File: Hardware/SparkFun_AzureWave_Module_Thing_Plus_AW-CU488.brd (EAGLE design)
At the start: 22.9 x 77.5 mm, 123 parts, among them J1 THING_PLUS, J3 QWIIC_RA, J5 USB-C, Q1 3.1A/30V/105mΩ, Q2 MBT3904DW1T1, U2 CP210X, U3 AP2112K-3.3V, U4 MCP73831

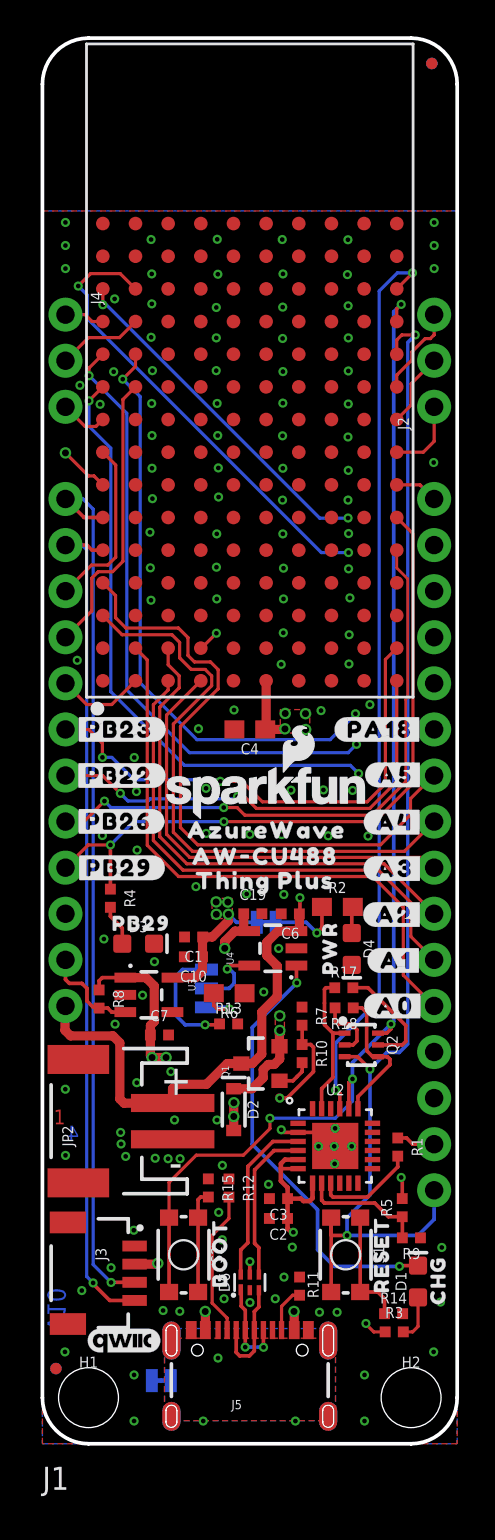
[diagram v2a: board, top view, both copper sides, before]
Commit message: changes found during proto testing
-removed R14 pulldown on reset button. It now pulls down directly to GND when pressed.
-adjusted Charge LED resistor to lower brightness (R3 changed from 1K to 4.7K)
-Added PTH header breakouts for UART LOG RX and TX.
-Changed silk on all pins to more user-friendly/common digital numbers.
-Added jumpers to more easily remove auto-boot circuit if needed for advanced use cases
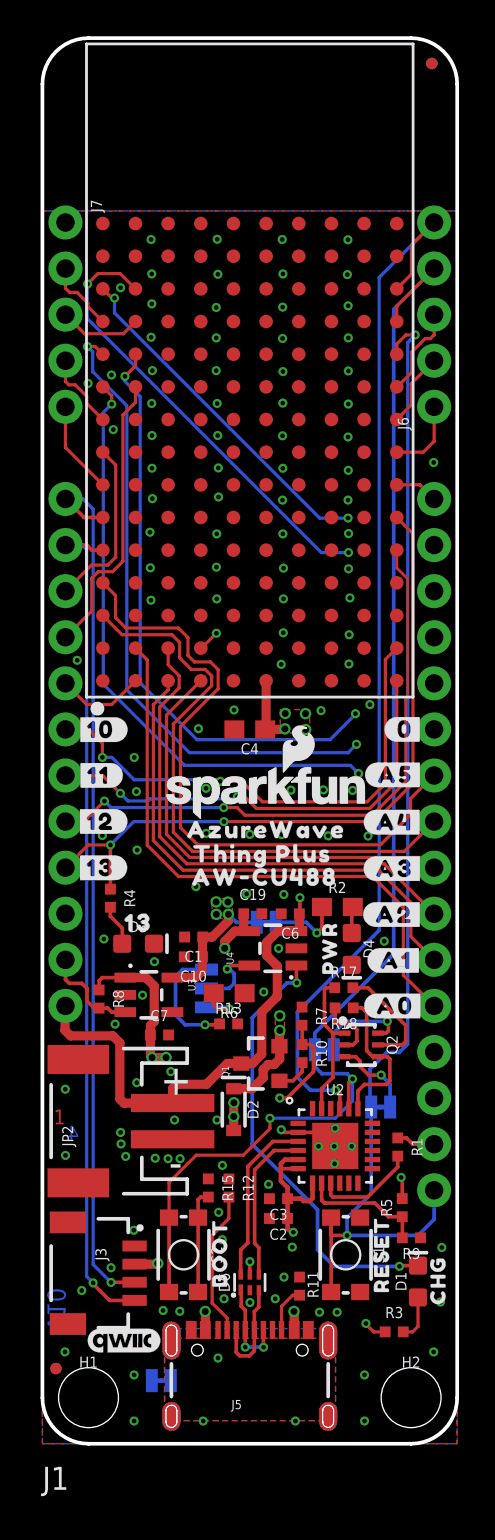
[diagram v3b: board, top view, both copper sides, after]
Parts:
- removed J2, J4: (no value), SparkFun-Connectors:1X03_NO_SILK
- removed R14: 10k, SparkFun-Resistors:0402-TIGHT
- removed TP1: (no value), SparkFun-Connectors:TP_15TH
- removed U$19: (no value), output:#PA4#32
- removed U$21: (no value), output:#PA2#32
- removed U$22: (no value), output:#PA14#32
- removed U$24: (no value), output:#PA15#32
- removed U$25: (no value), output:#PA26#SDA#32
- removed U$26: (no value), output:#PA25#SCL#32
- removed U$28: (no value), output:#PA30#32
- removed U$30: (no value), output:#PB3#A6#0
- removed U$31: (no value), output:#PA19#CS#32
- removed U$33: (no value), output:#PA27#32
- removed U$34: (no value), output:#PB23#32
- removed U$35: (no value), output:PB290
- removed U$36: (no value), output:#PB22#32
- removed U$37: (no value), output:#PB26#32
- removed U$38: (no value), output:#PB29#32
- removed U$39: (no value), output:#PA18#SCK#19
- removed U$40: (no value), output:#PA16#PICO#19
- removed U$44: (no value), output:#NC#0
- removed U$47: (no value), output:#PA17#POCI#19
- removed U$51: (no value), output:#PB4#A0#5
- removed U$52: (no value), output:#PB5#A1#5
- removed U$58: (no value), output:#PA18#6
- removed U$61: (no value), output:#PB6#A2#19
- removed U$63: (no value), output:#PB7#A3#19
- removed U$65: (no value), output:#PB1#A4#19
- removed U$66: (no value), output:#PB2#A5#19
- added J6, J7: (no value), SparkFun-Connectors:1X05_NO_SILK
- added JP1, JP3: (no value), SparkFun-Jumpers:SMT-JUMPER_2_NC_TRACE_SILK
- added U$48: (no value), output:#4#TX1#14
- added U$49: (no value), output:#3#RX1#14
- added U$50: (no value), output:#2#POCI#14
- added U$64: (no value), output:#1#PICO#14
- added U$67: (no value), output:#13#14
- added U$68: (no value), output:#12#14
- added U$69: (no value), output:#11#14
- added U$70: (no value), output:#10#14
- added U$71: (no value), output:#9#A6#14
- added U$72: (no value), output:#8#CS#14
- added U$73: (no value), output:#7#14
- added U$74: (no value), output:#6#SCL#14
- added U$75: (no value), output:#5#SDA#14
- added U$76: (no value), output:#0#SCK#14
- added U$77: (no value), output:#14#A0#15
- added U$80: (no value), output:#15#A1#15
- added U$81: (no value), output:#16#A2#16
- added U$82: (no value), output:#17#A3#17
- added U$83: (no value), output:#18#A4#18
- added U$84: (no value), output:#19#A5#19
- added U$85: (no value), output:#20#20
- added U$86: (no value), output:#GND#0
- added U$87: (no value), output:#21#21
- added U$88: (no value), output:#22#22
- added U$89: (no value), output:#23#23
- added U$90: (no value), output:#24#TX#24
- added U$91: (no value), output:#25#RX#25
- added U$92: (no value), output:#26#26
- added U$93: (no value), output:#27#27
- added U$94: (no value), output:#28#28
- added U$95: (no value), output:#29#29
- R3: value 1k -> 4.7k
- U$1: device output:#PA13#RXD#19 -> output:#10#30
- U$12: device output:#PA0#32 -> output:#12#30
- U$14: device output:#PB31#19 -> output:#13#30
- U$15: device output:#PB26#30 -> output:#JP1#1
- U$16: device output:#PB22#30 -> output:#0#1
- U$17: device output:#PB23#30 -> output:#JP3#2
- U$5: device output:#PA12#TXD#19 -> output:#11#30
- U$7: device output:#PB29#0 -> output:1330
- moved LOGO2 49.5 mm to (11.4, 10.2)
- moved U$12 27.7 mm to (3.21, 34.3), flipped to the top
- moved U$14 25.6 mm to (3.20, 31.7), flipped to the top
- moved U$15 19.6 mm to (15.9, 18.6), flipped to the bottom
- moved U$17 19.6 mm to (12.7, 21.7), flipped to the bottom
- moved U$5 18.5 mm to (3.10, 36.8), flipped to the top
- moved U$16 16.0 mm to (20.0, 39.4)
- moved U$1 15.4 mm to (3.22, 39.4), flipped to the top
- moved U$9 8.86 mm to (11.5, 56.6)
- moved U$8 7.87 mm to (11.4, 59.7)
- moved U$10 5.06 mm to (11.2, 58.2)
- moved U$7 3.22 mm to (5.29, 28.7)
- moved U$62 1.48 mm to (12.3, 32.5)
- moved U$27 1.15 mm to (12.4, 31.2)
- moved LOGO3 1.15 mm to (11.4, 71.4)
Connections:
- new net N$6: JP1.1, Q2.3
- net CHIP_EN: now also JP1.2; no longer Q2.3
- net GND: now also J7.1, S1.3, S1.4; no longer R14.2
- net N$10: now also JP3.1, Q2.6; no longer R14.1, S1.3, S1.4
- net PA0: now also J6.1; no longer J2.1
- net PA14: now also J7.2; no longer J4.1
- net PA15: now also J7.3; no longer J4.2
- net PA2: now also J6.3; no longer J2.3
- net PA27: now also J7.4; no longer J4.3
- net PA28: now also J7.5; no longer TP1.1
- net PA4: now also J6.2; no longer J2.2
- net PA7/UART-LOG-TXD: now also J6.4, JP3.2; no longer Q2.6
- net PA8/UART-LOG-RXD: now also J6.5
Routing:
- net PA8/UART-LOG-RXD: track 49.7 -> 58.3 mm, vias 2 -> 1
- net PA7/UART-LOG-TXD: track 67.2 -> 74.1 mm, vias 4 -> 2
- net N$6: track 0.00 -> 4.58 mm, vias 0 -> 1
- net PA28: track 2.79 -> 5.15 mm
- net PA14: track 2.22 -> 4.01 mm
- net CHIP_EN: track 67.9 -> 66.1 mm, vias 3 -> 2
- net PA27: track 2.67 -> 4.30 mm
- net PA16/PICO: track 39.6 -> 40.8 mm
- net N$10: track 6.42 -> 5.32 mm, vias 0 -> 1
- net RTS: track 7.88 -> 8.59 mm
- net LP_UART_RXD: track 31.1 -> 30.5 mm
- net GND: vias 134 -> 129

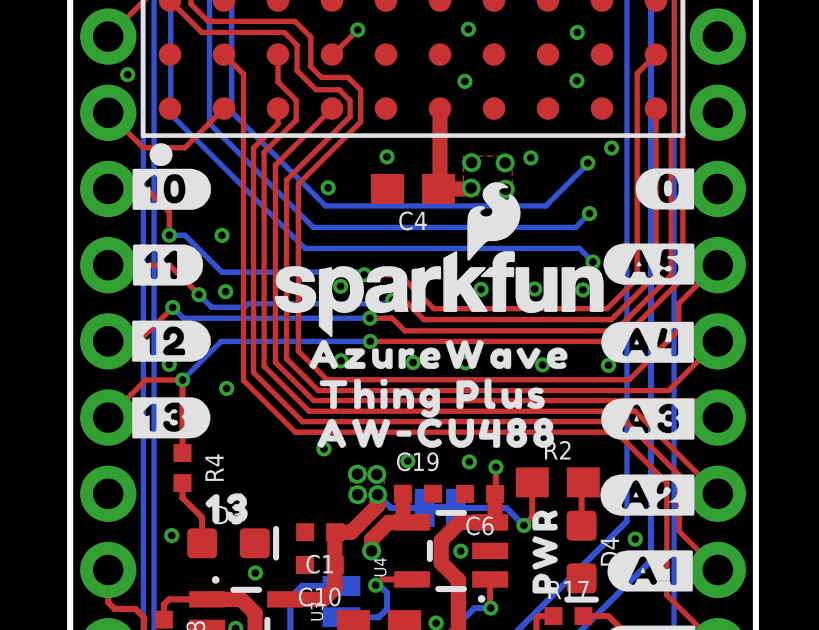
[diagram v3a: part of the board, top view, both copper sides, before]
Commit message: centered SFE logo and product name text
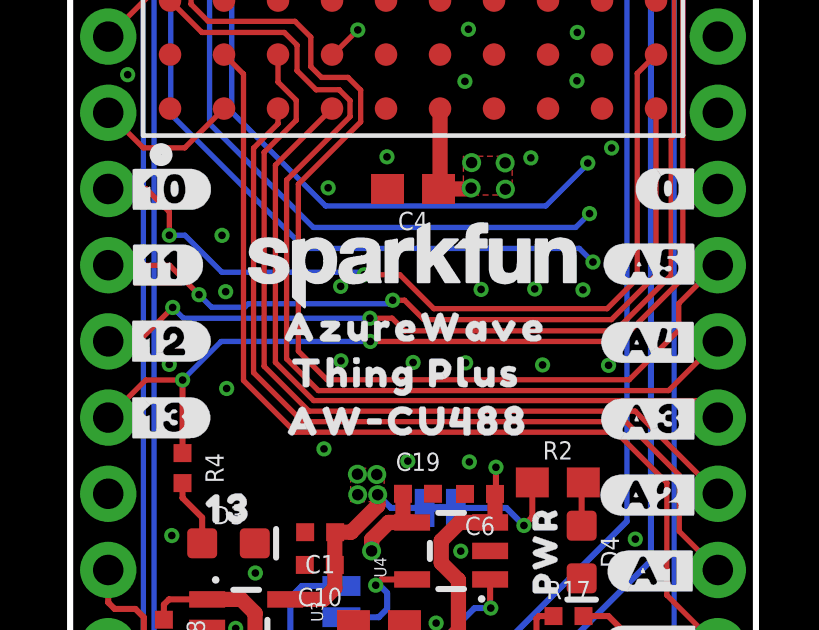
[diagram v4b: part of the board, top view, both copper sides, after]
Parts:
- removed LOGO3, LOGO5: SFE_LOGO_NAME_FLAME.1_INCH, SparkFun-Aesthetics:SFE_LOGO_NAME_FLAME_.1
- added LOGO1: SFE_LOGO_NAME.1_INCH, SparkFun-Aesthetics:SFE_LOGO_NAME_.1
- moved U$6 1.24 mm to (11.5, 34.8)
- moved U$62 1.17 mm to (11.4, 33.2)
- moved U$27 1.07 mm to (11.4, 31.6)
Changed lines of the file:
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@@
 <attribute name="VALUE" value="100k" x="2.697478125" y="24.546559375" size="0.6096" layer="27" font="vector" ratio="20" rot="R270" align="top-center"/>
 </element>
-<element name="LOGO3" library="SparkFun-Aesthetics" package="SFE_LOGO_NAME_FLAME_.1" value="SFE_LOGO_NAME_FLAME.1_INCH" x="11.43" y="71.371459375" smashed="yes" rot="MR0"/>
 <element name="LOGO4" library="SparkFun-Aesthetics" package="FOUR_LAYER_WARNING" value="FOUR_LAYER_WARNING" x="30.48" y="39.37" smashed="yes"/>
 <element name="U$59" library="SparkFun-Aesthetics" package="ORDERING_INSTRUCTIONS" value="" x="29.21" y="50.8" smashed="yes"/>
@@
 <element name="U$60" library="output" package="#100#0" value="" x="9.0297" y="26.41091875" smashed="yes" rot="MR90"/>
 <element name="U$4" library="output" package="#500#0" value="" x="9.0271625" y="23.7388375" smashed="yes" rot="MR90"/>
-<element name="U$62" library="output" package="THING_PLUS_0" value="" x="12.31138125" y="32.50945625" smashed="yes"/>
+<element name="U$62" library="output" package="THING_PLUS_0" value="" x="11.39444375" y="33.23335625" smashed="yes"/>
 <element name="R10" library="SparkFun-Resistors" package="0402-TIGHT" value="100" x="14.315440625" y="21.503640625" smashed="yes" rot="R270">
 <attribute name="NAME" x="15.077440625" y="21.503640625" size="0.6096" layer="25" font="vector" ratio="20" rot="R270" align="bottom-center"/>
@@
 <attribute name="VALUE" x="11.43" y="40.132" size="0.6096" layer="27" font="vector" ratio="20" rot="R180" align="top-center"/>
 </element>
-<element name="U$27" library="output" package="AW#CU488_0" value="" x="12.4307625" y="31.2166" smashed="yes"/>
+<element name="U$27" library="output" package="AW#CU488_0" value="" x="11.442703125" y="31.623" smashed="yes"/>
 <element name="U$2" library="output" package="BOOT0" value="" x="9.779" y="10.5156" smashed="yes" rot="R90"/>
-<element name="U$6" library="output" package="AZUREWAVE0" value="" x="12.346940625" y="33.842959375" smashed="yes"/>
+<element name="U$6" library="output" package="AZUREWAVE0" value="" x="11.521440625" y="34.762440625" smashed="yes"/>
 <element name="U$8" library="output" package="AZUREWAVE0" value="" x="11.43" y="59.69" smashed="yes" rot="MR0"/>
 <element name="U$9" library="output" package="AW#CU488_0" value="" x="11.452859375" y="56.57595625" smashed="yes" rot="MR0"/>
@@
 <element name="U$56" library="output" package="#A4#6" value="" x="19.4183" y="34.25698125" smashed="yes"/>
 <element name="U$57" library="output" package="#A5#6" value="" x="19.46401875" y="36.8655625" smashed="yes"/>
-<element name="LOGO5" library="SparkFun-Aesthetics" package="SFE_LOGO_NAME_FLAME_.1" value="SFE_LOGO_NAME_FLAME.1_INCH" x="12.38758125" y="35.892740625" smashed="yes"/>
 <element name="U$18" library="output" package="#A0#30" value="" x="19.453859375" y="24.127459375" smashed="yes"/>
 <element name="USBSHLD" library="SparkFun-Jumpers" package="SMT-JUMPER_2_NC_TRACE_SILK" package3d_urn="urn:adsk.eagle:package:39281/1" value="" x="6.5532" y="3.4798" smashed="yes" rot="MR180">
@@
 <element name="U$15" library="output" package="#JP1#1" value="" x="15.935959375" y="18.557240625" smashed="yes" rot="MR0"/>
 <element name="U$17" library="output" package="#JP3#2" value="" x="12.71778125" y="21.676359375" smashed="yes" rot="MR0"/>
+<element name="LOGO1" library="SparkFun-Aesthetics" package="SFE_LOGO_NAME_.1" value="SFE_LOGO_NAME.1_INCH" x="11.43" y="36.83" smashed="yes"/>
 </elements>
 <signals>

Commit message: Reds review catches
-added note in SCH about pwr LED jumper
-approved jumper overlap DRC errors
-added table lines to schematic info about auto-reset
-moved OSHW logo over via
-removed unncessary GND vias under USB-C
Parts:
- moved LOGO2 0.12 mm to (11.4, 10.0)
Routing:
- net GND: vias 129 -> 127
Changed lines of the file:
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@@
 <layer number="98" name="Guide" color="6" fill="1" visible="no" active="no"/>
 <layer number="99" name="SpiceOrder" color="7" fill="1" visible="no" active="no"/>
-<layer number="100" name="Muster" color="7" fill="1" visible="no" active="yes"/>
+<layer number="100" name="Muster" color="7" fill="1" visible="yes" active="yes"/>
 <layer number="101" name="Patch_Top" color="12" fill="4" visible="no" active="no"/>
 <layer number="102" name="Vscore" color="7" fill="1" visible="no" active="no"/>
@@
 <attribute name="VALUE" x="11.577315625" y="29.6926" size="0.6096" layer="27" font="vector" ratio="20" rot="R180" align="top-center"/>
 </element>
-<element name="LOGO2" library="SparkFun-Aesthetics" package="OSHW-LOGO-MINI" value="OSHW-LOGOMINI" x="11.43" y="10.16" smashed="yes" rot="MR0"/>
+<element name="LOGO2" library="SparkFun-Aesthetics" package="OSHW-LOGO-MINI" value="OSHW-LOGOMINI" x="11.43" y="10.0431625" smashed="yes" rot="MR0"/>
 <element name="J3" library="SparkFun-Connectors" package="JST04_1MM_RA" value="QWIIC_RA" x="5.08" y="9.398" smashed="yes" rot="R270">
 <attribute name="NAME" x="2.921" y="10.795" size="0.6096" layer="25" font="vector" ratio="20" rot="R270"/>
@@
 <via x="17.752059375" y="1.25221875" extent="1-16" drill="0.254"/>
 <via x="21.562059375" y="5.06221875" extent="1-16" drill="0.254"/>
-<via x="13.942059375" y="1.25221875" extent="1-16" drill="0.254"/>
-<via x="8.862059375" y="1.25221875" extent="1-16" drill="0.254"/>
 <via x="5.052059375" y="1.25221875" extent="1-16" drill="0.254"/>
 <via x="1.242059375" y="5.06221875" extent="1-16" drill="0.254"/>

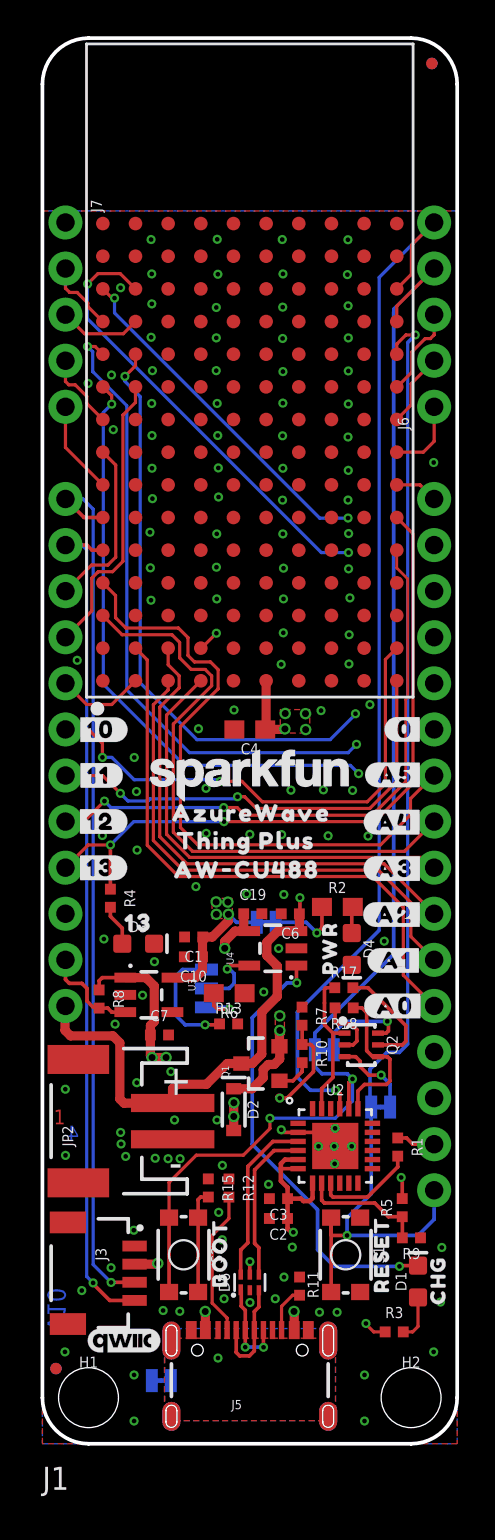
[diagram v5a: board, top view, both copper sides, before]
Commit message: more changes from reds review
-auto-reset disable jumpers changed to JP1 and JP2
-added more measures to top pht header on header rows
-swapped vreg from ap2112 to XC6222
-Add SFE LOGO to bottom silk
-more gnd vias near potential gnd loops
-fixed acid traps
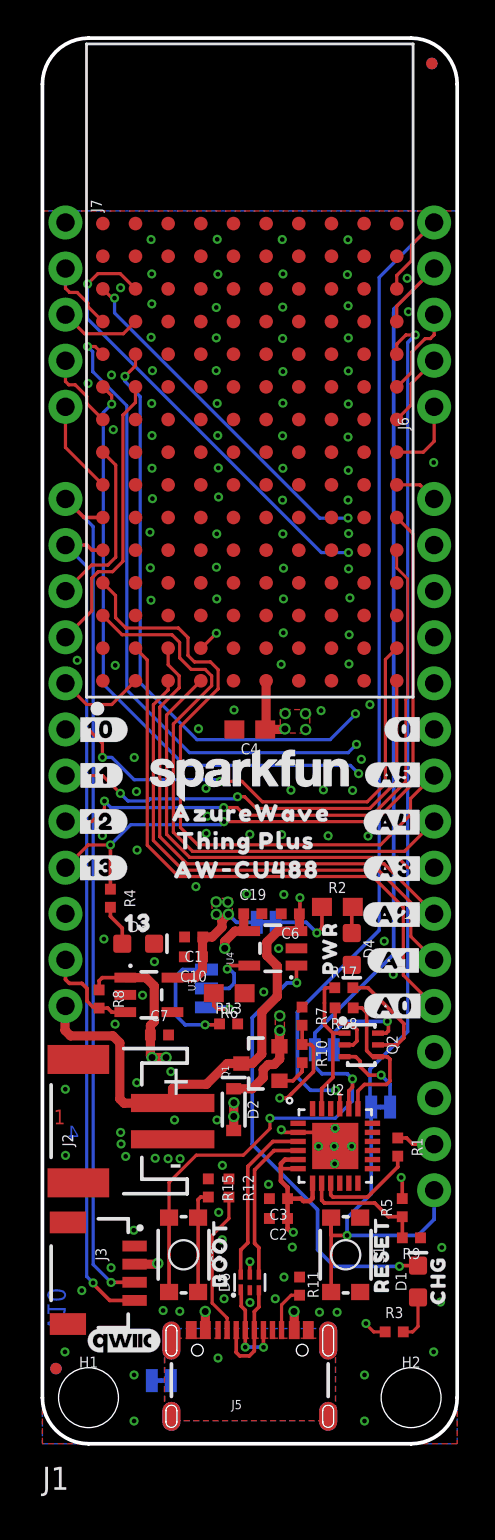
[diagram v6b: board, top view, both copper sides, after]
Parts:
- removed JP3: (no value), SparkFun-Jumpers:SMT-JUMPER_2_NC_TRACE_SILK
- removed U$17: (no value), output:#JP3#2
- added J2: LiPo, SparkFun-Connectors:JST-2-SMD
- added LOGO3: SFE_LOGO_NAME_FLAME.1_INCH, SparkFun-Aesthetics:SFE_LOGO_NAME_FLAME_.1
- added U$19: (no value), output:#JP2#4
- JP2: value LiPo -> (none); device SparkFun-Connectors:JST-2-SMD -> SparkFun-Jumpers:SMT-JUMPER_2_NC_TRACE_SILK
- U3: value AP2112K-3.3V -> XC6222B331MR-G
- moved JP2 12.7 mm to (15.5, 21.7), flipped to the bottom, turned to 0 degrees
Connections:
- net GND: now also J2.1; no longer JP2.1
- net N$10: now also JP2.1; no longer JP3.1
- net PA7/UART-LOG-TXD: now also JP2.2; no longer JP3.2
- net V_BATT: now also J2.2; no longer JP2.2
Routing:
- net PA26/SDA: track 48.6 -> 48.0 mm
- net PA25/SCL: track 46.7 -> 46.2 mm
- net GND: vias 127 -> 133

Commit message: AW-CU488 library work
-removed NC pin
-took "$" out of part name attribute
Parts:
- renumbered U$13 to U1
